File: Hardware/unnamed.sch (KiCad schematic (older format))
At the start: 156 parts, among them J1 USB2_C_Receptacle, SW1 SW_Push, SW2 Rotary_Encoder_Switch, SW3 Rotary_Encoder_Switch, SW4 Rotary_Encoder_Switch, U1 ATmega32U4-AU, U2 SRV05-4, Y1 16MHz

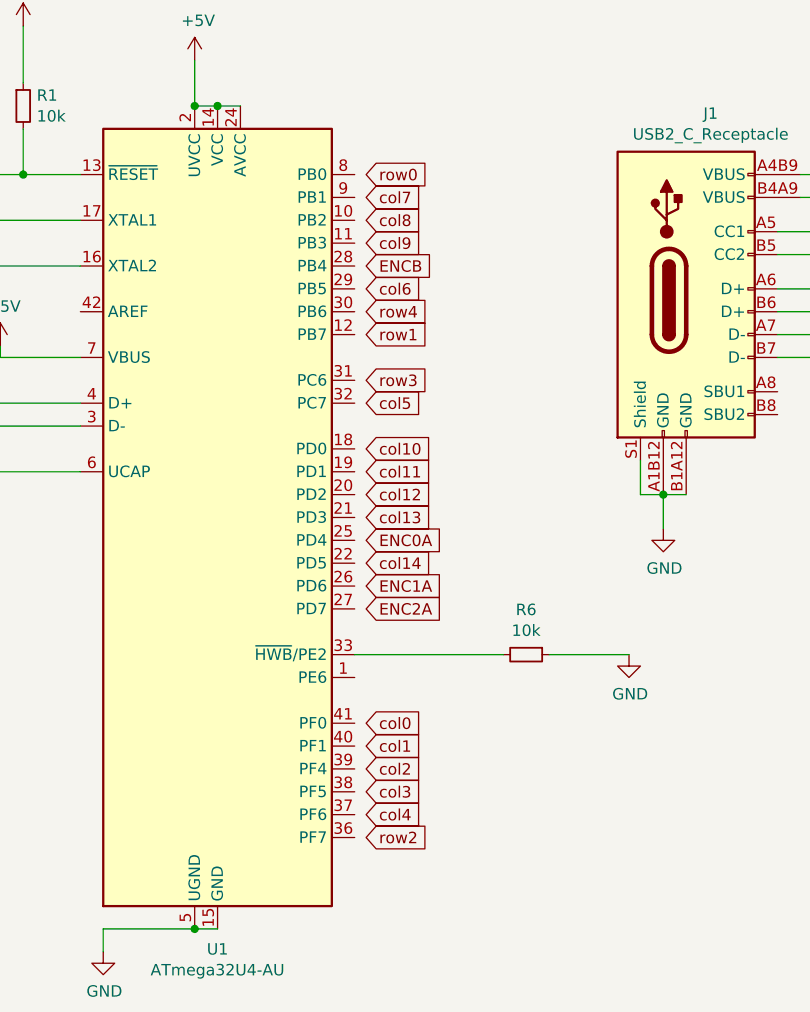
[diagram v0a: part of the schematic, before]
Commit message: Wire MCU + GND fill
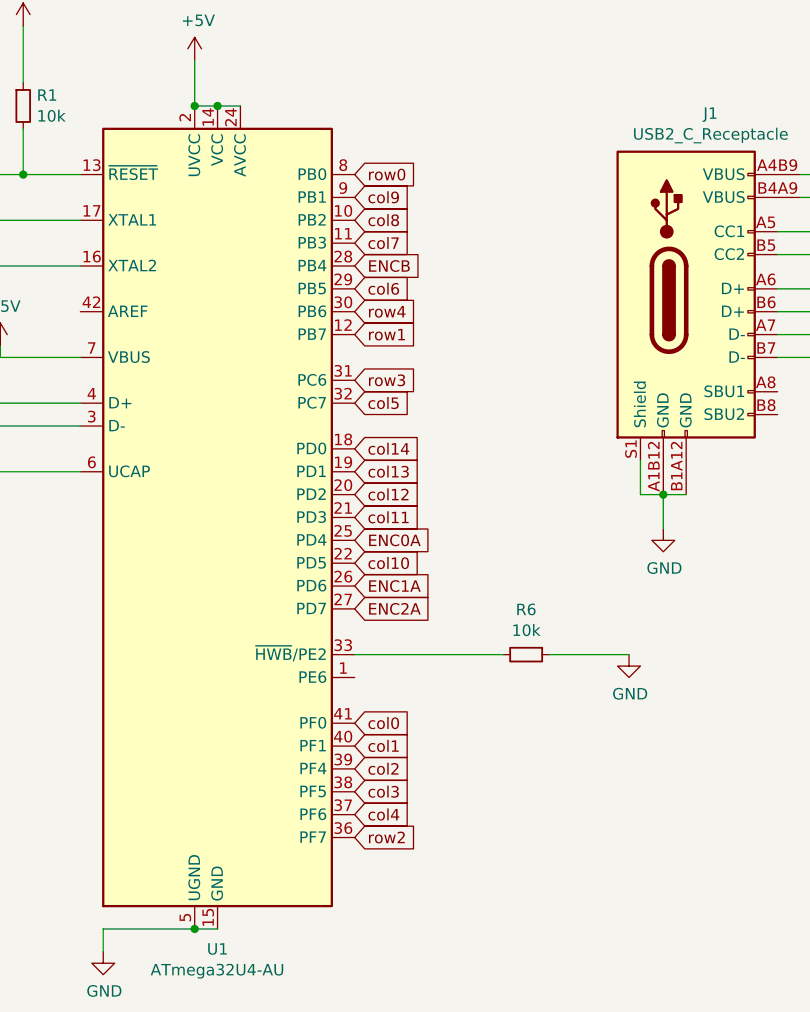
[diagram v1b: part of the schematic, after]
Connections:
- net 0col: now also U1.18 (PD0)
- net ENC0A: now also U1.25 (PD4)
- net ENC1A: now also U1.26 (PD6)
- net ENC2A: now also U1.27 (PD7)
- net ENCB: now also U1.28 (PB4)
- net col0: now also U1.41 (PF0)
- net col1: now also U1.40 (PF1)
- net col10: now also U1.22 (PD5)
- net col11: now also U1.21 (PD3)
- net col12: now also U1.20 (PD2)
- net col13: now also U1.19 (PD1)
- net col2: now also U1.39 (PF4)
- net col3: now also U1.38 (PF5)
- net col4: now also U1.37 (PF6)
- net col5: now also U1.32 (PC7)
- net col6: now also U1.29 (PB5)
- net col7: now also U1.11 (PB3)
- net col8: now also U1.10 (PB2)
- net col9: now also U1.9 (PB1)
- net row0: now also U1.8 (PB0)
- net row1: now also U1.12 (PB7)
- net row2: now also U1.36 (PF7)
- net row3: now also U1.31 (PC6)
- net row4: now also U1.30 (PB6)
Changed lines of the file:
@@
 Wire Wire Line
 	8450 3050 8600 3050
-Text GLabel 5550 5400 2    50   Input ~ 0
+Text GLabel 5500 5400 2    50   Input ~ 0
 col0
-Text GLabel 5550 5500 2    50   Input ~ 0
+Text GLabel 5500 5500 2    50   Input ~ 0
 col1
-Text GLabel 5550 5600 2    50   Input ~ 0
+Text GLabel 5500 5600 2    50   Input ~ 0
 col2
-Text GLabel 5550 5700 2    50   Input ~ 0
+Text GLabel 5500 5700 2    50   Input ~ 0
 col3
-Text GLabel 5550 5800 2    50   Input ~ 0
+Text GLabel 5500 5800 2    50   Input ~ 0
 col4
-Text GLabel 5550 4000 2    50   Input ~ 0
+Text GLabel 5500 4000 2    50   Input ~ 0
 col5
-Text GLabel 5550 3500 2    50   Input ~ 0
+Text GLabel 5500 3500 2    50   Input ~ 0
 col6
-Text GLabel 5550 3100 2    50   Input ~ 0
+Text GLabel 5500 3300 2    50   Input ~ 0
 col7
-Text GLabel 5550 3200 2    50   Input ~ 0
+Text GLabel 5500 3200 2    50   Input ~ 0
 col8
-Text GLabel 5550 3300 2    50   Input ~ 0
+Text GLabel 5500 3100 2    50   Input ~ 0
 col9
-Text GLabel 5550 4200 2    50   Input ~ 0
+Text GLabel 5500 4700 2    50   Input ~ 0
 col10
-Text GLabel 5550 4300 2    50   Input ~ 0
+Text GLabel 5500 4500 2    50   Input ~ 0
 col11
-Text GLabel 5550 4400 2    50   Input ~ 0
+Text GLabel 5500 4400 2    50   Input ~ 0
 col12
-Text GLabel 5550 4500 2    50   Input ~ 0
+Text GLabel 5500 4300 2    50   Input ~ 0
 col13
-Text GLabel 5550 4700 2    50   Input ~ 0
+Text GLabel 5500 4200 2    50   Input ~ 0
 col14
-Text GLabel 5550 3000 2    50   Input ~ 0
+Text GLabel 5500 3000 2    50   Input ~ 0
 row0
-Text GLabel 5550 3700 2    50   Input ~ 0
+Text GLabel 5500 3700 2    50   Input ~ 0
 row1
-Text GLabel 5550 5900 2    50   Input ~ 0
+Text GLabel 5500 5900 2    50   Input ~ 0
 row2
-Text GLabel 5550 3900 2    50   Input ~ 0
+Text GLabel 5500 3900 2    50   Input ~ 0
 row3
-Text GLabel 5550 3600 2    50   Input ~ 0
+Text GLabel 5500 3600 2    50   Input ~ 0
 row4
 $Comp
@@
 Text GLabel 20000 10300 0    50   Input ~ 0
 ENC2A
-Text GLabel 5550 3400 2    50   Input ~ 0
+Text GLabel 5500 3400 2    50   Input ~ 0
 ENCB
-Text GLabel 5550 4600 2    50   Input ~ 0
+Text GLabel 5500 4600 2    50   Input ~ 0
 ENC0A
-Text GLabel 5550 4800 2    50   Input ~ 0
+Text GLabel 5500 4800 2    50   Input ~ 0
 ENC1A
-Text GLabel 5550 4900 2    50   Input ~ 0
+Text GLabel 5500 4900 2    50   Input ~ 0
 ENC2A
 Connection ~ 19550 9500
